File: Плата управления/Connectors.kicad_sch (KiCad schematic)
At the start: 6 parts, among them J1 Conn_01x10, J2 Conn_01x10, J3 Conn_01x02, J4 A, J5 B, J6 C

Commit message: Расставил драйвера
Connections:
- net A: now also J2.8 (Pin_8); no longer J1.8 (Pin_8)
- net B: now also J2.1 (Pin_1); no longer J1.1 (Pin_1)
- net C: now also J1.9 (Pin_9)
- net G1: now also J2.7 (Pin_7); no longer J1.7 (Pin_7)
- net G2: now also J2.3 (Pin_3); no longer J1.3 (Pin_3)
- net G3: now also J2.2 (Pin_2); no longer J1.2 (Pin_2)
- net G4: now also J1.4 (Pin_4)
- net G5: now also J1.10 (Pin_10)
- net G6: now also J1.6 (Pin_6)
- net GND: now also J1.2 (Pin_2), J1.3 (Pin_3), J1.5 (Pin_5), J1.8 (Pin_8), J2.4 (Pin_4), J2.6 (Pin_6); no longer J1.4 (Pin_4), J1.6 (Pin_6)
- net Shunt_1: now also J2.10 (Pin_10); no longer J1.10 (Pin_10)
- net Shunt_2: now also J2.9 (Pin_9); no longer J1.9 (Pin_9)
- net Temp_A: now also J2.5 (Pin_5); no longer J1.5 (Pin_5)
- net Temp_B: now also J1.1 (Pin_1)
- net Temp_C: now also J1.7 (Pin_7)
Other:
- moved on the sheet: J1, J2
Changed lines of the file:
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@@
     )
   )
-  (symbol (lib_id "Connector_Generic:Conn_01x10") (at 106.68 83.82 0) (unit 1)
-    (in_bom yes) (on_board yes) (dnp no) (fields_autoplaced)
-    (property "Reference" "J2" (at 109.22 83.82 0)
-      (effects (font (size 1.27 1.27)) (justify left))
-    )
-    (property "Value" "Conn_01x10" (at 109.22 86.36 0)
-      (effects (font (size 1.27 1.27)) (justify left))
-    )
-    (property "Footprint" "Connector_PinSocket_2.54mm:PinSocket_1x10_P2.54mm_Vertical_SMD_Pin1Right" (at 106.68 83.82 0)
-      (effects (font (size 1.27 1.27)) hide)
-    )
-    (property "Datasheet" "~" (at 106.68 83.82 0)
+  (symbol (lib_id "Connector_Generic:Conn_01x10") (at 106.68 54.61 0) (unit 1)
+    (in_bom yes) (on_board yes) (dnp no) (fields_autoplaced)
+    (property "Reference" "J2" (at 109.22 54.61 0)
+      (effects (font (size 1.27 1.27)) (justify left))
+    )
+    (property "Value" "Conn_01x10" (at 109.22 57.15 0)
+      (effects (font (size 1.27 1.27)) (justify left))
+    )
+    (property "Footprint" "Connector_PinSocket_2.54mm:PinSocket_1x10_P2.54mm_Vertical_SMD_Pin1Right" (at 106.68 54.61 0)
+      (effects (font (size 1.27 1.27)) hide)
+    )
+    (property "Datasheet" "~" (at 106.68 54.61 0)
       (effects (font (size 1.27 1.27)) hide)
     )
@@
     )
   )
-  (symbol (lib_id "Connector_Generic:Conn_01x10") (at 106.68 54.61 0) (unit 1)
-    (in_bom yes) (on_board yes) (dnp no) (fields_autoplaced)
-    (property "Reference" "J1" (at 109.22 54.61 0)
-      (effects (font (size 1.27 1.27)) (justify left))
-    )
-    (property "Value" "Conn_01x10" (at 109.22 57.15 0)
-      (effects (font (size 1.27 1.27)) (justify left))
-    )
-    (property "Footprint" "Connector_PinSocket_2.54mm:PinSocket_1x10_P2.54mm_Vertical_SMD_Pin1Left" (at 106.68 54.61 0)
-      (effects (font (size 1.27 1.27)) hide)
-    )
-    (property "Datasheet" "~" (at 106.68 54.61 0)
-      (effects (font (size 1.27 1.27)) hide)
-    )
+  (symbol (lib_id "Connector_Generic:Conn_01x10") (at 106.68 85.09 0) (unit 1)
+    (in_bom yes) (on_board yes) (dnp no) (fields_autoplaced)
+    (property "Reference" "J1" (at 109.22 85.09 0)
+      (effects (font (size 1.27 1.27)) (justify left))
+    )
+    (property "Value" "Conn_01x10" (at 109.22 87.63 0)
+      (effects (font (size 1.27 1.27)) (justify left))
+    )
+    (property "Footprint" "Connector_PinSocket_2.54mm:PinSocket_1x10_P2.54mm_Vertical_SMD_Pin1Left" (at 106.68 85.09 0)
+      (effects (font (size 1.27 1.27)) hide)
+    )
+    (property "Datasheet" "~" (at 106.68 85.09 0)
+      (effects (font (size 1.27 1.27)) hide)
+    )

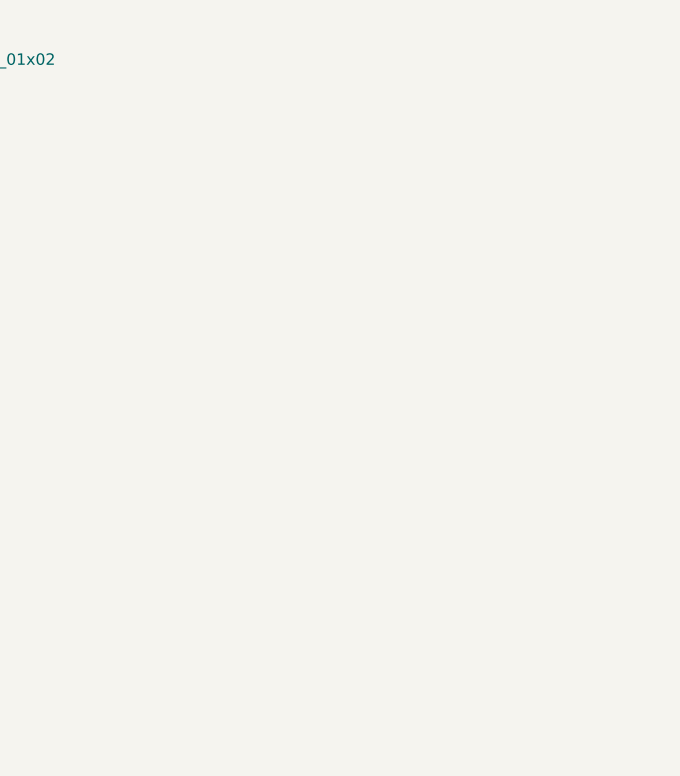
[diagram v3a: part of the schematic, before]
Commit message: Расставил компоненты по плате
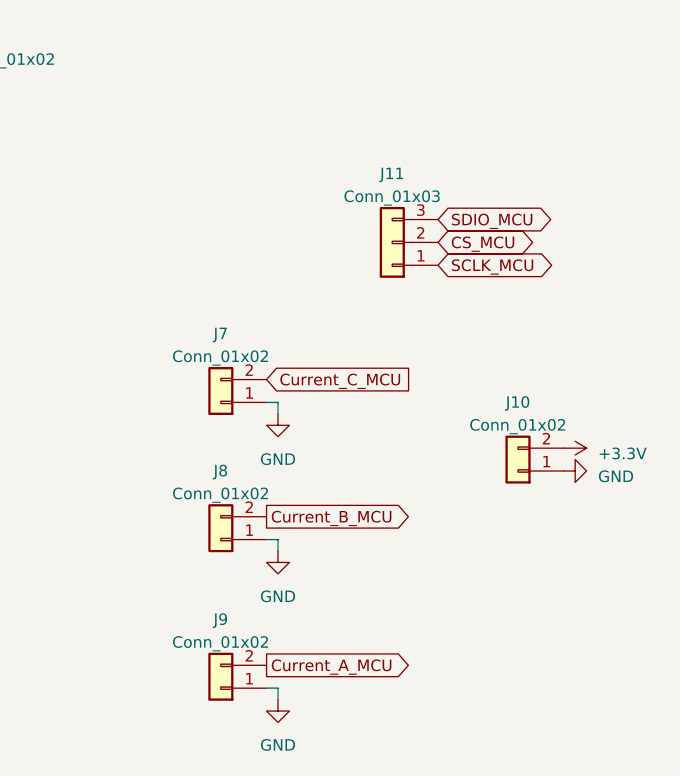
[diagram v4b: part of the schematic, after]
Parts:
- added J10, J7, J8, J9: Conn_01x02, Connector_PinHeader_2.54mm:PinHeader_1x02_P2.54mm_Vertical_SMD_Pin1Left, symbol Connector_Generic:Conn_01x02
- added J11: Conn_01x03, Connector_PinHeader_2.54mm:PinHeader_1x03_P2.54mm_Vertical_SMD_Pin1Left, symbol Connector_Generic:Conn_01x03
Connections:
- net GND: now also J10.1 (Pin_1), J7.1 (Pin_1), J8.1 (Pin_1), J9.1 (Pin_1)
- new net +3.3V: J10.2 (Pin_2)
- new net CS_MCU: J11.2 (Pin_2)
- new net Current_A_MCU: J9.2 (Pin_2)
- new net Current_B_MCU: J8.2 (Pin_2)
- new net Current_C_MCU: J7.2 (Pin_2)
- new net SCLK_MCU: J11.1 (Pin_1)
- new net SDIO_MCU: J11.3 (Pin_3)

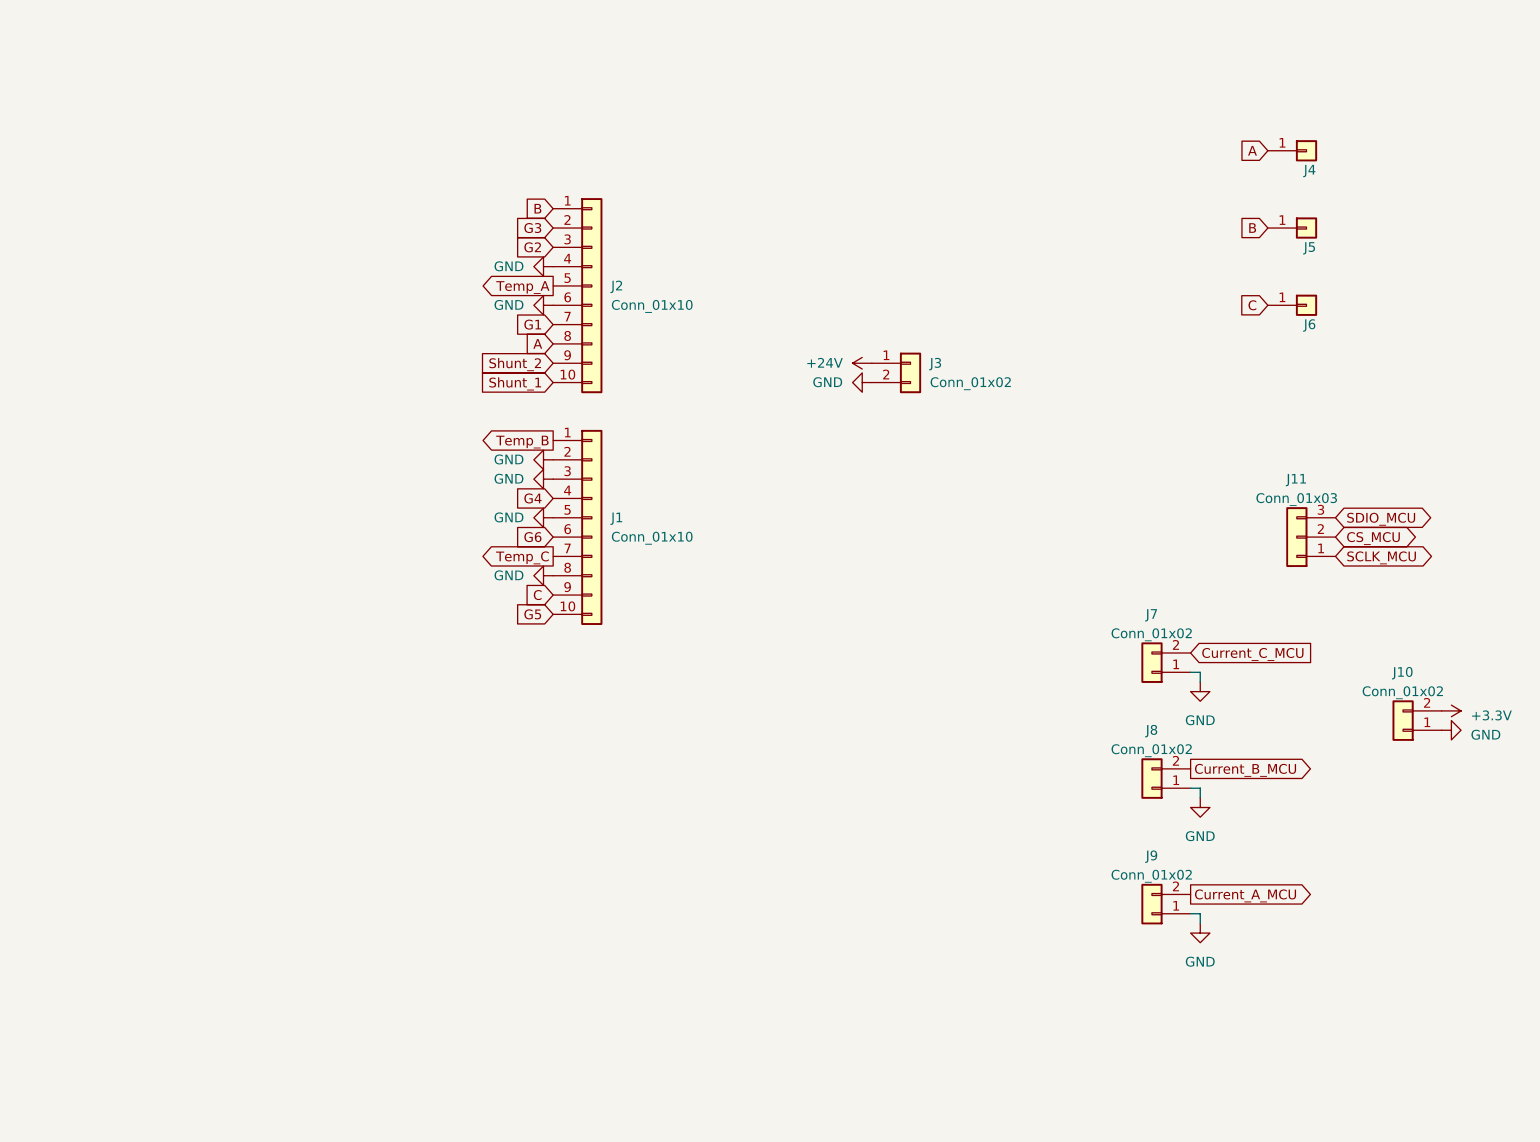
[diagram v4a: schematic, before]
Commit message: Изменил контур под новую крышку
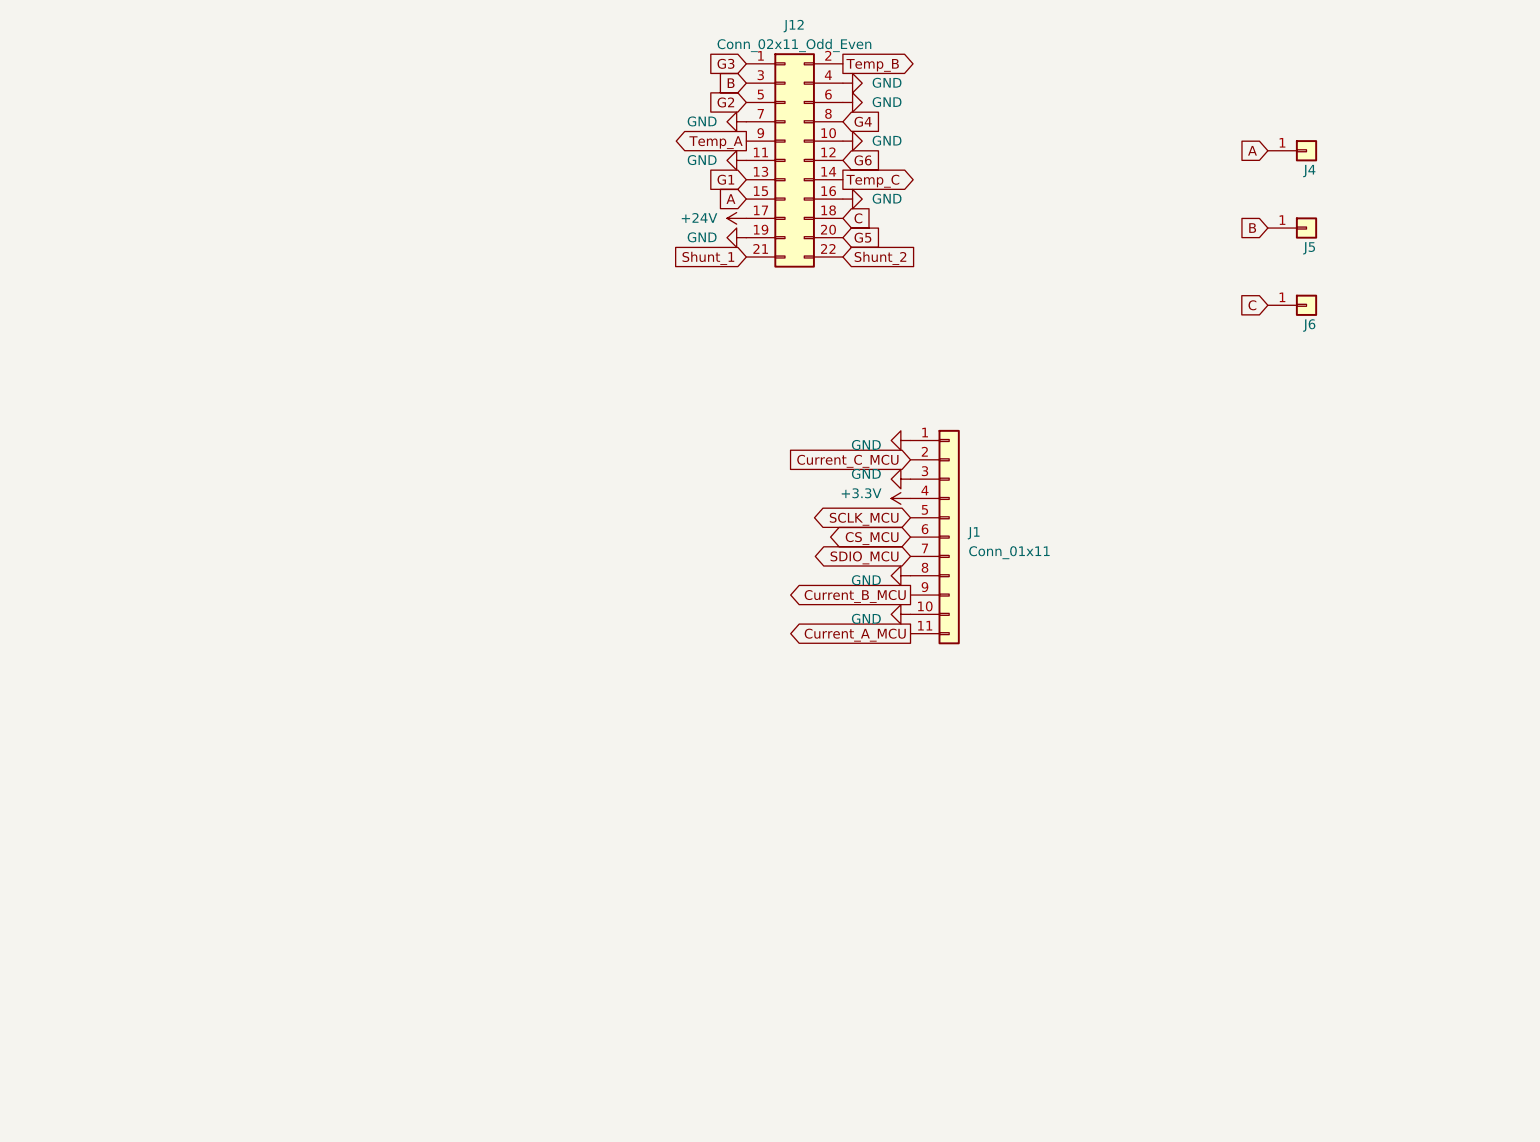
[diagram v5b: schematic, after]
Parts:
- removed J1: Conn_01x10, Connector_PinSocket_2.54mm:PinSocket_1x10_P2.54mm_Vertical_SMD_Pin1Left, symbol Connector_Generic:Conn_01x10
- removed J10, J7, J8, J9: Conn_01x02, Connector_PinHeader_2.54mm:PinHeader_1x02_P2.54mm_Vertical_SMD_Pin1Left, symbol Connector_Generic:Conn_01x02
- removed J11: Conn_01x03, Connector_PinHeader_2.54mm:PinHeader_1x03_P2.54mm_Vertical_SMD_Pin1Left, symbol Connector_Generic:Conn_01x03
- removed J2: Conn_01x10, Connector_PinSocket_2.54mm:PinSocket_1x10_P2.54mm_Vertical_SMD_Pin1Right, symbol Connector_Generic:Conn_01x10
- removed J3: Conn_01x02, Connector_PinSocket_2.54mm:PinSocket_1x02_P2.54mm_Vertical_SMD_Pin1Left, symbol Connector_Generic:Conn_01x02
- added J1: Conn_01x11, Connector_PinHeader_2.54mm:PinHeader_1x11_P2.54mm_Vertical, symbol Connector_Generic:Conn_01x11
- added J12: Conn_02x11_Odd_Even, Connector_PinHeader_2.54mm:PinHeader_2x11_P2.54mm_Vertical_SMD, symbol Connector_Generic:Conn_02x11_Odd_Even
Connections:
- net +24V: now also J12.17 (Pin_17)
- net +3.3V: now also J1.4 (Pin_4)
- net A: now also J12.15 (Pin_15)
- net B: now also J12.3 (Pin_3)
- net C: now also J12.18 (Pin_18)
- net CS_MCU: now also J1.6 (Pin_6)
- net Current_A_MCU: now also J1.11 (Pin_11)
- net Current_B_MCU: now also J1.9 (Pin_9)
- net Current_C_MCU: now also J1.2 (Pin_2)
- net G1: now also J12.13 (Pin_13)
- net G2: now also J12.5 (Pin_5)
- net G3: now also J12.1 (Pin_1)
- net G4: now also J12.8 (Pin_8)
- net G5: now also J12.20 (Pin_20)
- net G6: now also J12.12 (Pin_12)
- net GND: now also J1.1 (Pin_1), J1.10 (Pin_10), J1.3 (Pin_3), J1.8 (Pin_8), J12.10 (Pin_10), J12.11 (Pin_11), J12.16 (Pin_16), J12.19 (Pin_19), J12.4 (Pin_4), J12.6 (Pin_6), J12.7 (Pin_7)
- net SCLK_MCU: now also J1.5 (Pin_5)
- net SDIO_MCU: now also J1.7 (Pin_7)
- net Shunt_1: now also J12.21 (Pin_21)
- net Shunt_2: now also J12.22 (Pin_22)
- net Temp_A: now also J12.9 (Pin_9)
- net Temp_B: now also J12.2 (Pin_2)
- net Temp_C: now also J12.14 (Pin_14)

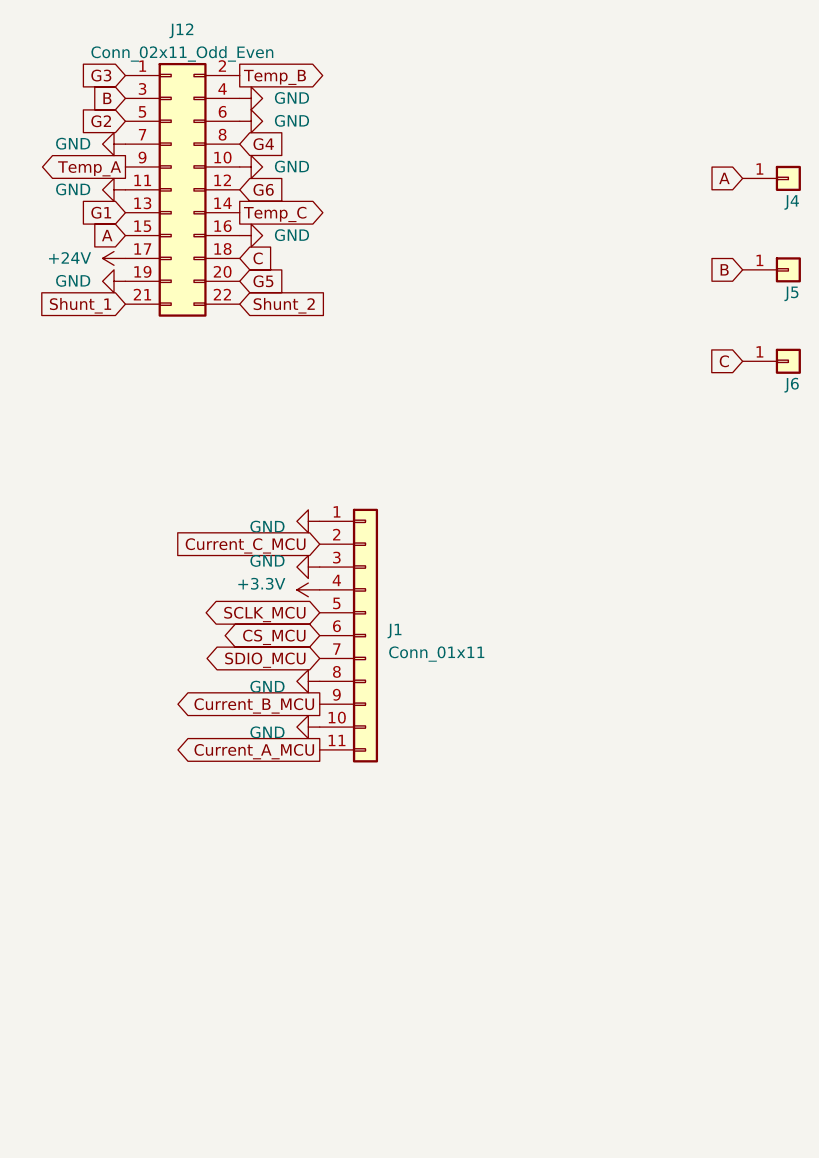
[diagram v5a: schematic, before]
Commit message: Добавил разъёмы под интерфейсы
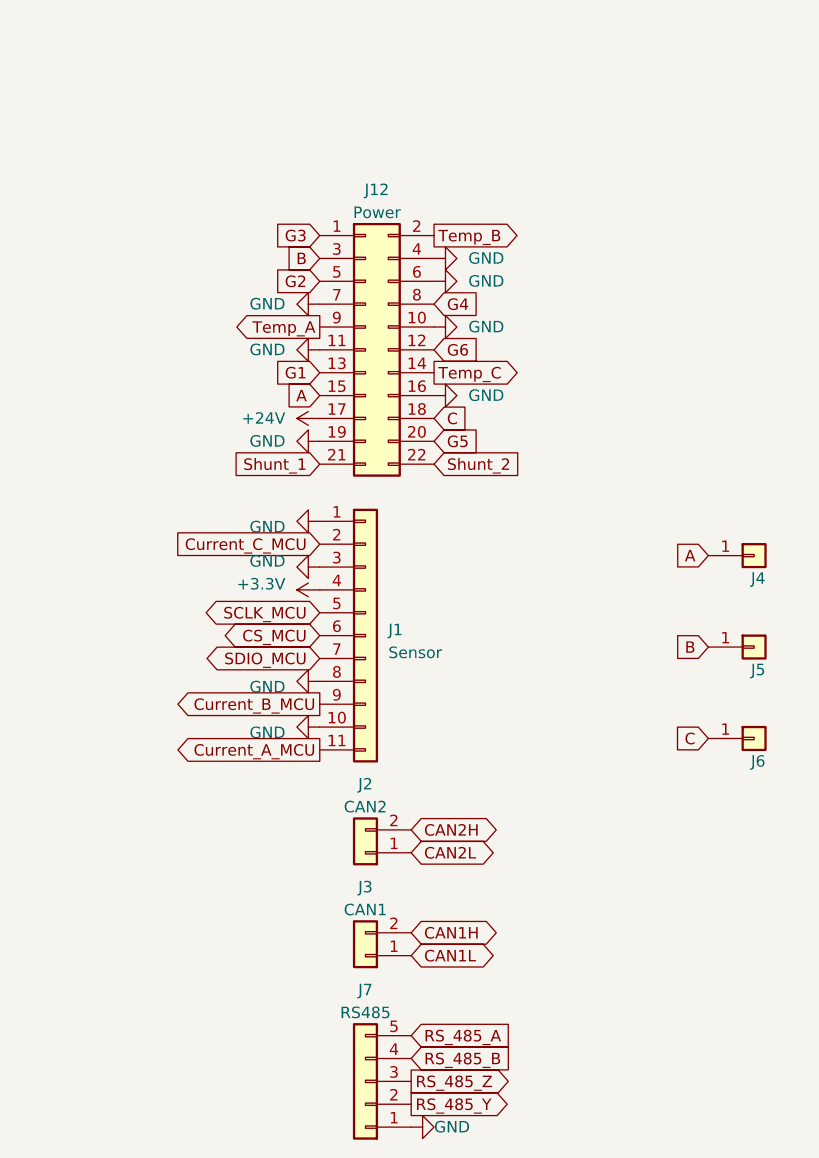
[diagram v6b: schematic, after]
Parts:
- added J2: CAN2, Connector_Molex:Molex_PicoBlade_53048-0210_1x02_P1.25mm_Horizontal, symbol Connector_Generic:Conn_01x02
- added J3: CAN1, Connector_Molex:Molex_PicoBlade_53048-0210_1x02_P1.25mm_Horizontal, symbol Connector_Generic:Conn_01x02
- added J7: RS485, Connector_Molex:Molex_PicoBlade_53048-0510_1x05_P1.25mm_Horizontal, symbol Connector_Generic:Conn_01x05
- J1: value Conn_01x11 -> Sensor
- J12: value Conn_02x11_Odd_Even -> Power
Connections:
- net GND: now also J7.1 (Pin_1)
- new net CAN1H: J3.2 (Pin_2)
- new net CAN1L: J3.1 (Pin_1)
- new net CAN2H: J2.2 (Pin_2)
- new net CAN2L: J2.1 (Pin_1)
- new net RS_485_A: J7.5 (Pin_5)
- new net RS_485_B: J7.4 (Pin_4)
- new net RS_485_Y: J7.2 (Pin_2)
- new net RS_485_Z: J7.3 (Pin_3)
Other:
- moved on the sheet: J12, J4, J5, J6

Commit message: Новый контур платы
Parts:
- removed J1: Sensor, Connector_PinHeader_2.54mm:PinHeader_1x11_P2.54mm_Vertical, symbol Connector_Generic:Conn_01x11
- added J1: RS485, Connector_Molex:Molex_PicoBlade_53048-0510_1x05_P1.25mm_Horizontal, symbol Connector_Generic:Conn_01x05
- added J10, J8: Conn_02x03_Odd_Even, Connector_PinHeader_2.54mm:PinHeader_2x03_P2.54mm_Vertical_SMD, symbol Connector_Generic:Conn_02x03_Odd_Even
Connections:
- net +3.3V: now also J8.4 (Pin_4)
- net CS_MCU: now also J8.3 (Pin_3)
- net Current_A_MCU: now also J8.6 (Pin_6)
- net Current_B_MCU: now also J10.3 (Pin_3)
- net Current_C_MCU: now also J10.1 (Pin_1)
- net GND: now also J1.1 (Pin_1), J10.2 (Pin_2), J8.2 (Pin_2)
- net SCLK_MCU: now also J8.1 (Pin_1)
- net SDIO_MCU: now also J8.5 (Pin_5)
- new net Analog_Input1: J1.5 (Pin_5)
- new net Analog_Input2: J1.4 (Pin_4)
- new net Digital_input1: J1.3 (Pin_3)
- new net Digital_input2: J1.2 (Pin_2)
- new net Temp_Coil1: J10.5 (Pin_5)
- new net Temp_Coil2: J10.6 (Pin_6)
- new net Temp_Coil3: J10.4 (Pin_4)
